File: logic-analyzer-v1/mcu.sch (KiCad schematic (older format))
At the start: 31 parts

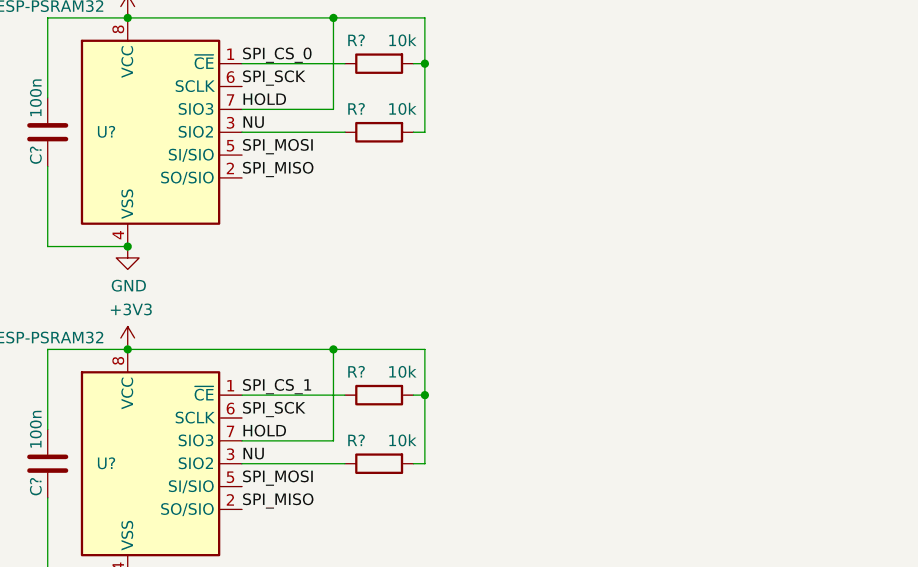
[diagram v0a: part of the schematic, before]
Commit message: adding 2x spi memory
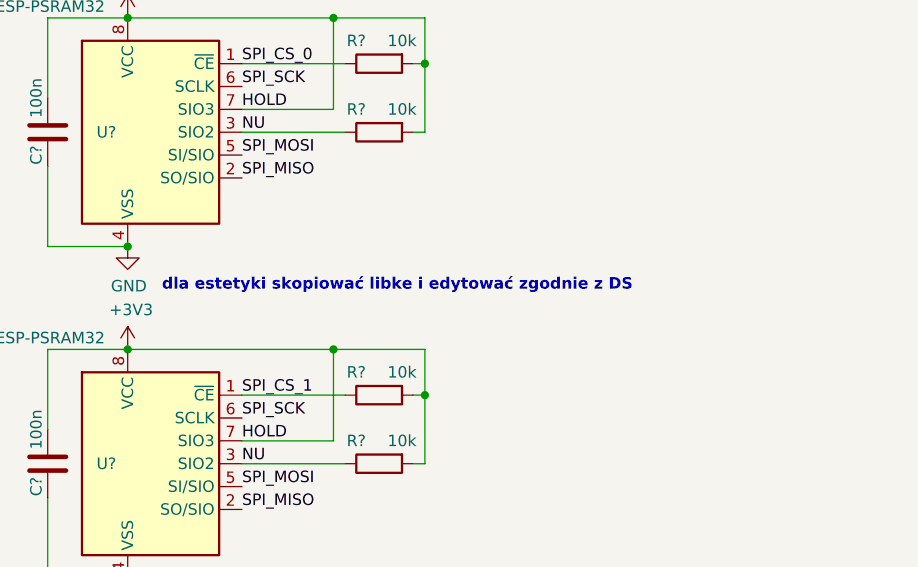
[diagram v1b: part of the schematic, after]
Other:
- note added: "dla estetyki skopiować libke i edytować zgodnie z DS"
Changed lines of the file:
@@
 Wire Bus Line
 	4900 3400 4900 4200
+Text Notes 1500 6150 0    50   ~ 10
+dla estetyki skopiować libke i edytować zgodnie z DS
 $EndSCHEMATC

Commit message: update 03.2021
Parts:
- removed C? (x2): 100n, Capacitor_SMD:C_0603_1608Metric_Pad1.05x0.95mm_HandSolder, symbol Device:C
- removed R? (x4): 10k, Resistor_SMD:R_0603_1608Metric_Pad1.05x0.95mm_HandSolder, symbol Device:R
- removed U? (x2): ESP-PSRAM32, Package_SO:SOIC-8_3.9x4.9mm_P1.27mm, symbol Memory_RAM:ESP-PSRAM32
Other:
- note removed: "dla estetyki skopiować libke i edytować zgodnie z DS"
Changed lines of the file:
@@
 $Descr A4 11693 8268
 encoding utf-8
-Sheet 3 3
+Sheet 6 6
 Title ""
 Date ""
@@
 Text Label 6800 3700 0    50   ~ 0
 SPI_CS_1
-Text HLabel 7250 3600 2    50   BiDi ~ 0
+Text HLabel 7250 3600 2    50   Output ~ 0
 SPI_CS_0
-Text HLabel 7250 3700 2    50   BiDi ~ 0
+Text HLabel 7250 3700 2    50   Output ~ 0
 SPI_CS_1
-$Comp
-L Memory_RAM:ESP-PSRAM32 U?
-U 1 1 5F44BD22
-P 1450 5450
-F 0 "U?" H 1300 5450 50  0000 R CNN
-F 1 "ESP-PSRAM32" H 1250 6000 50  0000 R CNN
-F 2 "Package_SO:SOIC-8_3.9x4.9mm_P1.27mm" H 1450 4850 50  0001 C CNN
-F 3 "https://www.espressif.com/sites/default/files/documentation/esp-psram32_datasheet_en.pdf" H 1050 5950 50  0001 C CNN
-	1    1450 5450
-	1    0    0    -1
-$EndComp
-$Comp
-L power:+3V3 #PWR?
-U 1 1 5F4518F5
-P 1350 4950
-F 0 "#PWR?" H 1350 4800 50  0001 C CNN
-F 1 "+3V3" H 1365 5123 50  0000 C CNN
-F 2 "" H 1350 4950 50  0001 C CNN
-F 3 "" H 1350 4950 50  0001 C CNN
-	1    1350 4950
-	1    0    0    -1
-$EndComp
-$Comp
-L power:GND #PWR?
-U 1 1 5F46E3B9
-P 1350 5950
-F 0 "#PWR?" H 1350 5700 50  0001 C CNN
-F 1 "GND" H 1355 5777 50  0000 C CNN
-F 2 "" H 1350 5950 50  0001 C CNN
-F 3 "" H 1350 5950 50  0001 C CNN
-	1    1350 5950
-	1    0    0    -1
-$EndComp
 NoConn ~ 5400 3300
 NoConn ~ 5400 3400
-Text Label 1850 5550 0    50   ~ 0
-SPI_MOSI
-Text Label 1850 5650 0    50   ~ 0
-SPI_MISO
-Text Label 1850 5250 0    50   ~ 0
-SPI_SCK
-Text Label 1850 5150 0    50   ~ 0
-SPI_CS_0
-Text Label 1850 5350 0    50   ~ 0
-HOLD
-$Comp
-L Device:R R?
-U 1 1 5F4D563F
-P 2450 5450
-AR Path="/5F08ED8D/5F4D563F" Ref="R?"  Part="1"
-AR Path="/5F19654C/5F4D563F" Ref="R?"  Part="1"
-F 0 "R?" V 2350 5550 50  0000 C CNN
-F 1 "10k" V 2350 5350 50  0000 C CNN
-F 2 "Resistor_SMD:R_0603_1608Metric_Pad1.05x0.95mm_HandSolder" V 2380 5450 50  0001 C CNN
-F 3 "~" H 2450 5450 50  0001 C CNN
-	1    2450 5450
-	0    -1   1    0
-$EndComp
-$Comp
-L Device:R R?
-U 1 1 5F4D5C5E
-P 2450 5150
-AR Path="/5F08ED8D/5F4D5C5E" Ref="R?"  Part="1"
-AR Path="/5F19654C/5F4D5C5E" Ref="R?"  Part="1"
-F 0 "R?" V 2350 5250 50  0000 C CNN
-F 1 "10k" V 2350 5050 50  0000 C CNN
-F 2 "Resistor_SMD:R_0603_1608Metric_Pad1.05x0.95mm_HandSolder" V 2380 5150 50  0001 C CNN
-F 3 "~" H 2450 5150 50  0001 C CNN
-	1    2450 5150
-	0    -1   1    0
-$EndComp
-Wire Wire Line
-	1850 5350 2250 5350
-Text Label 1850 5450 0    50   ~ 0
-NU
-Wire Wire Line
-	1850 5450 2300 5450
-Wire Wire Line
-	2650 4950 2650 5150
-Connection ~ 2650 5150
-Wire Wire Line
-	2650 5150 2650 5450
-Wire Wire Line
-	1350 4950 2250 4950
-Connection ~ 2250 4950
-Wire Wire Line
-	2250 4950 2650 4950
-Wire Wire Line
-	2600 5150 2650 5150
-Wire Wire Line
-	2600 5450 2650 5450
-Wire Wire Line
-	1850 5150 2300 5150
-Wire Wire Line
-	2250 4950 2250 5350
-$Comp
-L Device:C C?
-U 1 1 5F54203B
-P 1000 5450
-F 0 "C?" V 950 5350 50  0000 C CNN
-F 1 "100n" V 950 5600 50  0000 C CNN
-F 2 "Capacitor_SMD:C_0603_1608Metric_Pad1.05x0.95mm_HandSolder" H 1038 5300 50  0001 C CNN
-F 3 "~" H 1000 5450 50  0001 C CNN
-	1    1000 5450
-	1    0    0    -1
-$EndComp
-Wire Wire Line
-	1350 5950 1000 5950
-Wire Wire Line
-	1000 5950 1000 5600
-Wire Wire Line
-	1350 4950 1000 4950
-Wire Wire Line
-	1000 4950 1000 5300
-Connection ~ 1350 4950
-Connection ~ 1350 5950
-$Comp
-L Memory_RAM:ESP-PSRAM32 U?
-U 1 1 5F55C8F8
-P 1450 6900
-F 0 "U?" H 1300 6900 50  0000 R CNN
-F 1 "ESP-PSRAM32" H 1250 7450 50  0000 R CNN
-F 2 "Package_SO:SOIC-8_3.9x4.9mm_P1.27mm" H 1450 6300 50  0001 C CNN
-F 3 "https://www.espressif.com/sites/default/files/documentation/esp-psram32_datasheet_en.pdf" H 1050 7400 50  0001 C CNN
-	1    1450 6900
-	1    0    0    -1
-$EndComp
-$Comp
-L power:+3V3 #PWR?
-U 1 1 5F55C8FE
-P 1350 6400
-F 0 "#PWR?" H 1350 6250 50  0001 C CNN
-F 1 "+3V3" H 1365 6573 50  0000 C CNN
-F 2 "" H 1350 6400 50  0001 C CNN
-F 3 "" H 1350 6400 50  0001 C CNN
-	1    1350 6400
-	1    0    0    -1
-$EndComp
-$Comp
-L power:GND #PWR?
-U 1 1 5F55C904
-P 1350 7400
-F 0 "#PWR?" H 1350 7150 50  0001 C CNN
-F 1 "GND" H 1355 7227 50  0000 C CNN
-F 2 "" H 1350 7400 50  0001 C CNN
-F 3 "" H 1350 7400 50  0001 C CNN
-	1    1350 7400
-	1    0    0    -1
-$EndComp
-Text Label 1850 7000 0    50   ~ 0
-SPI_MOSI
-Text Label 1850 7100 0    50   ~ 0
-SPI_MISO
-Text Label 1850 6700 0    50   ~ 0
-SPI_SCK
-Text Label 1850 6600 0    50   ~ 0
-SPI_CS_1
-Text Label 1850 6800 0    50   ~ 0
-HOLD
-$Comp
-L Device:R R?
-U 1 1 5F55C915
-P 2450 6600
-AR Path="/5F08ED8D/5F55C915" Ref="R?"  Part="1"
-AR Path="/5F19654C/5F55C915" Ref="R?"  Part="1"
-F 0 "R?" V 2350 6700 50  0000 C CNN
-F 1 "10k" V 2350 6500 50  0000 C CNN
-F 2 "Resistor_SMD:R_0603_1608Metric_Pad1.05x0.95mm_HandSolder" V 2380 6600 50  0001 C CNN
-F 3 "~" H 2450 6600 50  0001 C CNN
-	1    2450 6600
-	0    -1   1    0
-$EndComp
-Wire Wire Line
-	1850 6800 2250 6800
-Text Label 1850 6900 0    50   ~ 0
-NU
-Wire Wire Line
-	2650 6400 2650 6600
-Connection ~ 2650 6600
-Wire Wire Line
-	2650 6600 2650 6900
-Wire Wire Line
-	1350 6400 2250 6400
-Connection ~ 2250 6400
-Wire Wire Line
-	2250 6400 2650 6400
-Wire Wire Line
-	2600 6600 2650 6600
-Wire Wire Line
-	1850 6600 2300 6600
-Wire Wire Line
-	2250 6400 2250 6800
-$Comp
-L Device:C C?
-U 1 1 5F55C928
-P 1000 6900
-F 0 "C?" V 950 6800 50  0000 C CNN
-F 1 "100n" V 950 7050 50  0000 C CNN
-F 2 "Capacitor_SMD:C_0603_1608Metric_Pad1.05x0.95mm_HandSolder" H 1038 6750 50  0001 C CNN
-F 3 "~" H 1000 6900 50  0001 C CNN
-	1    1000 6900
-	1    0    0    -1
-$EndComp
-Wire Wire Line
-	1350 7400 1000 7400
-Wire Wire Line
-	1000 7400 1000 7050
-Wire Wire Line
-	1350 6400 1000 6400
-Wire Wire Line
-	1000 6400 1000 6750
-Connection ~ 1350 6400
-Connection ~ 1350 7400
-Wire Wire Line
-	2600 6900 2650 6900
-Wire Wire Line
-	1850 6900 2300 6900
-$Comp
-L Device:R R?
-U 1 1 5F55C90F
-P 2450 6900
-AR Path="/5F08ED8D/5F55C90F" Ref="R?"  Part="1"
-AR Path="/5F19654C/5F55C90F" Ref="R?"  Part="1"
-F 0 "R?" V 2350 7000 50  0000 C CNN
-F 1 "10k" V 2350 6800 50  0000 C CNN
-F 2 "Resistor_SMD:R_0603_1608Metric_Pad1.05x0.95mm_HandSolder" V 2380 6900 50  0001 C CNN
-F 3 "~" H 2450 6900 50  0001 C CNN
-	1    2450 6900
-	0    -1   1    0
-$EndComp
 Wire Bus Line
 	4900 3400 4900 4200
-Text Notes 1500 6150 0    50   ~ 10
-dla estetyki skopiować libke i edytować zgodnie z DS
 $EndSCHEMATC

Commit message: MOD uart port direction, minor cosmetic changes
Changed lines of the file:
@@
 $Descr A4 11693 8268
 encoding utf-8
-Sheet 6 6
+Sheet 7 8
 Title ""
 Date ""
@@
 Text HLabel 7250 4800 2    50   BiDi ~ 0
 USB_DP
-Text HLabel 7250 3800 2    50   BiDi ~ 0
+Text HLabel 7250 3800 2    50   Output ~ 0
 USART2_TX
-Text HLabel 7250 3900 2    50   BiDi ~ 0
+Text HLabel 7250 3900 2    50   Input ~ 0
 USART2_RX
 Wire Bus Line

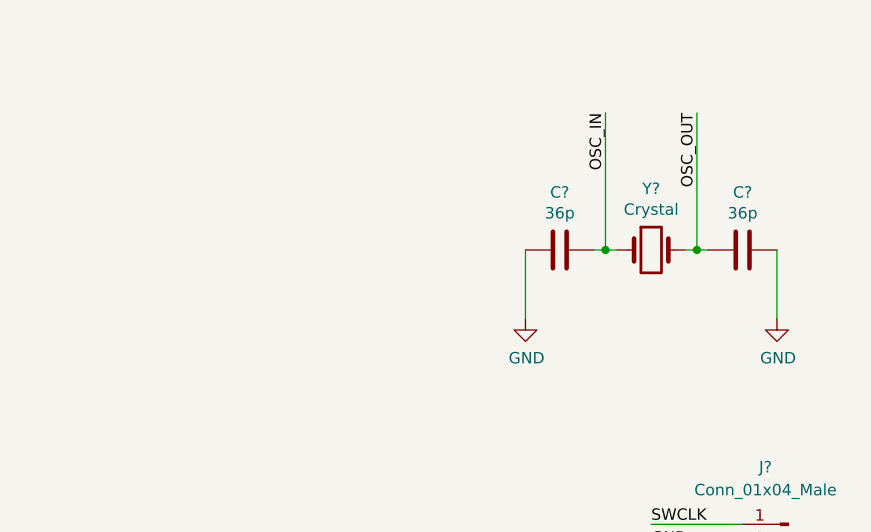
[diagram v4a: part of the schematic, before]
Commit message: changing sram blocks from new library
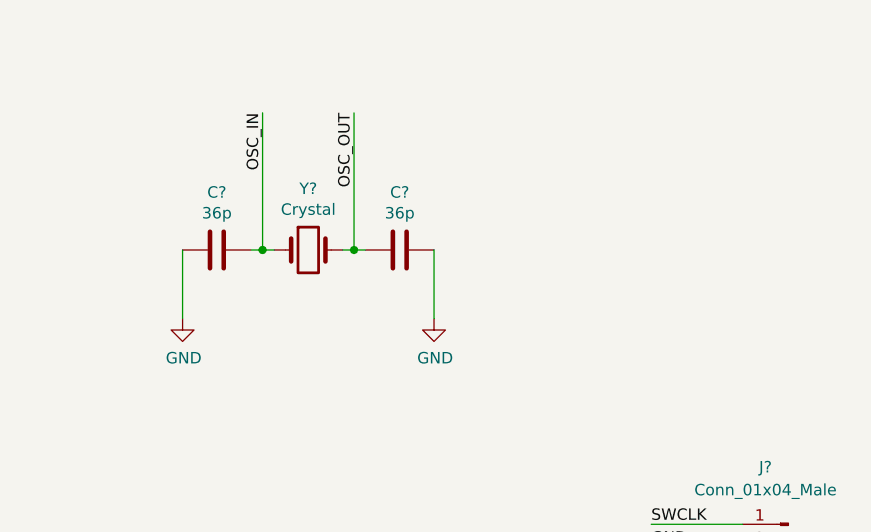
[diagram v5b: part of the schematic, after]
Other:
- moved on the sheet: C?, Y?
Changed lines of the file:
@@
 L Device:Crystal Y?
 U 1 1 5F19E72B
-P 10100 1600
-F 0 "Y?" H 10100 1868 50  0000 C CNN
-F 1 "Crystal" H 10100 1777 50  0000 C CNN
-F 2 "Crystal:Crystal_HC49-U_Vertical" H 10100 1600 50  0001 C CNN
-F 3 "https://www.tme.eu/Document/1a73b69e6487c12c6ef660d6ee951878/YIC-49US_49SMT-quartz_crystal.pdf" H 10100 1600 50  0001 C CNN
-F 4 "https://www.tme.eu/pl/details/48.00m-hc49-s/rezonatory-kwarcowe-tht/yic/" H 10100 1600 50  0001 C CNN "Shop"
-	1    10100 1600
+P 8600 1600
+F 0 "Y?" H 8600 1868 50  0000 C CNN
+F 1 "Crystal" H 8600 1777 50  0000 C CNN
+F 2 "Crystal:Crystal_HC49-U_Vertical" H 8600 1600 50  0001 C CNN
+F 3 "https://www.tme.eu/Document/1a73b69e6487c12c6ef660d6ee951878/YIC-49US_49SMT-quartz_crystal.pdf" H 8600 1600 50  0001 C CNN
+F 4 "https://www.tme.eu/pl/details/48.00m-hc49-s/rezonatory-kwarcowe-tht/yic/" H 8600 1600 50  0001 C CNN "Shop"
+	1    8600 1600
 	1    0    0    -1
 $EndComp
@@
 L Device:C C?
 U 1 1 5F19FA91
-P 9700 1600
-F 0 "C?" V 9448 1600 50  0000 C CNN
-F 1 "36p" V 9539 1600 50  0000 C CNN
-F 2 "Capacitor_SMD:C_0603_1608Metric_Pad1.05x0.95mm_HandSolder" H 9738 1450 50  0001 C CNN
-F 3 "~" H 9700 1600 50  0001 C CNN
-	1    9700 1600
+P 8200 1600
+F 0 "C?" V 7948 1600 50  0000 C CNN
+F 1 "36p" V 8039 1600 50  0000 C CNN
+F 2 "Capacitor_SMD:C_0603_1608Metric_Pad1.05x0.95mm_HandSolder" H 8238 1450 50  0001 C CNN
+F 3 "~" H 8200 1600 50  0001 C CNN
+	1    8200 1600
 	0    1    1    0
 $EndComp
@@
 L Device:C C?
 U 1 1 5F1A0D22
-P 10500 1600
-F 0 "C?" V 10248 1600 50  0000 C CNN
-F 1 "36p" V 10339 1600 50  0000 C CNN
-F 2 "Capacitor_SMD:C_0603_1608Metric_Pad1.05x0.95mm_HandSolder" H 10538 1450 50  0001 C CNN
-F 3 "~" H 10500 1600 50  0001 C CNN
-	1    10500 1600
+P 9000 1600
+F 0 "C?" V 8748 1600 50  0000 C CNN
+F 1 "36p" V 8839 1600 50  0000 C CNN
+F 2 "Capacitor_SMD:C_0603_1608Metric_Pad1.05x0.95mm_HandSolder" H 9038 1450 50  0001 C CNN
+F 3 "~" H 9000 1600 50  0001 C CNN
+	1    9000 1600
 	0    1    1    0
 $EndComp
@@
 OSC_OUT
 Wire Wire Line
-	9850 1600 9900 1600
-Text Label 9900 1000 3    50   ~ 0
+	8350 1600 8400 1600
+Text Label 8400 1000 3    50   ~ 0
 OSC_IN
-Text Label 10300 1000 3    50   ~ 0
+Text Label 8800 1000 3    50   ~ 0
 OSC_OUT
 $Comp
 L power:GND #PWR?
 U 1 1 5F3F1273
-P 9550 1900
-F 0 "#PWR?" H 9550 1650 50  0001 C CNN
-F 1 "GND" H 9555 1727 50  0000 C CNN
-F 2 "" H 9550 1900 50  0001 C CNN
-F 3 "" H 9550 1900 50  0001 C CNN
-	1    9550 1900
+P 8050 1900
+F 0 "#PWR?" H 8050 1650 50  0001 C CNN
+F 1 "GND" H 8055 1727 50  0000 C CNN
+F 2 "" H 8050 1900 50  0001 C CNN
+F 3 "" H 8050 1900 50  0001 C CNN
+	1    8050 1900
 	1    0    0    -1
 $EndComp
@@
 L power:GND #PWR?
 U 1 1 5F3F19A7
-P 10650 1900
-F 0 "#PWR?" H 10650 1650 50  0001 C CNN
-F 1 "GND" H 10655 1727 50  0000 C CNN
-F 2 "" H 10650 1900 50  0001 C CNN
-F 3 "" H 10650 1900 50  0001 C CNN
-	1    10650 1900
-	1    0    0    -1
-$EndComp
-Wire Wire Line
-	10650 1900 10650 1600
-Wire Wire Line
-	9550 1900 9550 1600
-Wire Wire Line
-	9900 1000 9900 1600
-Connection ~ 9900 1600
-Wire Wire Line
-	9900 1600 9950 1600
-Wire Wire Line
-	10300 1000 10300 1600
-Wire Wire Line
-	10250 1600 10300 1600
-Connection ~ 10300 1600
-Wire Wire Line
-	10300 1600 10350 1600
+P 9150 1900
+F 0 "#PWR?" H 9150 1650 50  0001 C CNN
+F 1 "GND" H 9155 1727 50  0000 C CNN
+F 2 "" H 9150 1900 50  0001 C CNN
+F 3 "" H 9150 1900 50  0001 C CNN
+	1    9150 1900
+	1    0    0    -1
+$EndComp
+Wire Wire Line
+	9150 1900 9150 1600
+Wire Wire Line
+	8050 1900 8050 1600
+Wire Wire Line
+	8400 1000 8400 1600
+Connection ~ 8400 1600
+Wire Wire Line
+	8400 1600 8450 1600
+Wire Wire Line
+	8800 1000 8800 1600
+Wire Wire Line
+	8750 1600 8800 1600
+Connection ~ 8800 1600
+Wire Wire Line
+	8800 1600 8850 1600
 $Comp
 L Device:R R?
